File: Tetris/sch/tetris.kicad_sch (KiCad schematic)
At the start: 36 parts, among them J1 SWD, SW1 Boot, SW4 Reset, U1 CH32V203C8T6, U4 TLV70433DBVR

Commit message: PCB routing in progress
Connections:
- net LED/S1: now also U1.19 (PB1/ADC9); no longer U1.18 (PB0/ADC8)
- net LED/S2: now also U1.18 (PB0/ADC8); no longer U1.19 (PB1/ADC9)
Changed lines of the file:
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@@
 	(wire
 		(pts
-			(xy 236.22 110.49) (xy 232.41 110.49)
-		)
-		(stroke
-			(width 0)
-			(type default)
-		)
-	)
-	(wire
-		(pts
 			(xy 254 58.42) (xy 257.81 58.42)
 		)
@@
 	(wire
 		(pts
-			(xy 238.76 107.95) (xy 232.41 107.95)
+			(xy 200.66 77.47) (xy 214.63 77.47)
 		)
 		(stroke
@@
 	(wire
 		(pts
-			(xy 200.66 77.47) (xy 214.63 77.47)
+			(xy 147.32 102.87) (xy 149.86 102.87)
 		)
 		(stroke
@@
 	(wire
 		(pts
-			(xy 147.32 102.87) (xy 149.86 102.87)
+			(xy 224.79 58.42) (xy 224.79 45.72)
 		)
 		(stroke
@@
 	(wire
 		(pts
-			(xy 224.79 58.42) (xy 224.79 45.72)
+			(xy 269.24 58.42) (xy 269.24 62.23)
 		)
 		(stroke
@@
 	(wire
 		(pts
-			(xy 269.24 58.42) (xy 269.24 62.23)
+			(xy 232.41 110.49) (xy 236.22 110.49)
 		)
 		(stroke
@@
 	(wire
 		(pts
+			(xy 232.41 107.95) (xy 238.76 107.95)
+		)
+		(stroke
+			(width 0)
+			(type default)
+		)
+	)
+	(wire
+		(pts
 			(xy 163.83 87.63) (xy 163.83 77.47)
 		)
@@
 		)
 		(pin "S1" output
-			(at 232.41 107.95 0)
+			(at 232.41 110.49 0)
 			(effects
 				(font
@@
 		)
 		(pin "S2" output
-			(at 232.41 110.49 0)
+			(at 232.41 107.95 0)
 			(effects
 				(font

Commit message: Tetris PCB route in progress
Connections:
- net at U1.34 (PA13/SWDIO): now also J1.3 (Pin_3); no longer J1.4 (Pin_4)
- net at U1.37 (PA14/SWCLK): now also J1.4 (Pin_4); no longer J1.3 (Pin_3)
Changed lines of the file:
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@@
+	(wire
+		(pts
+			(xy 163.83 60.96) (xy 177.8 60.96)
+		)
+		(stroke
+			(width 0)
+			(type default)
+		)
+	)
 	(wire
 		(pts
@@
 	(wire
 		(pts
-			(xy 161.29 49.53) (xy 161.29 58.42)
-		)
-		(stroke
-			(width 0)
-			(type default)
-		)
-	)
-	(wire
-		(pts
 			(xy 147.32 80.01) (xy 151.13 80.01)
 		)
@@
 	(wire
 		(pts
+			(xy 50.8 185.42) (xy 50.8 186.69)
+		)
+		(stroke
+			(width 0)
+			(type default)
+		)
+	)
+	(wire
+		(pts
+			(xy 96.52 50.8) (xy 96.52 54.61)
+		)
+		(stroke
+			(width 0)
+			(type default)
+		)
+	)
+	(wire
+		(pts
+			(xy 163.83 92.71) (xy 167.64 92.71)
+		)
+		(stroke
+			(width 0)
+			(type default)
+		)
+	)
+	(wire
+		(pts
+			(xy 254 53.34) (xy 260.35 53.34)
+		)
+		(stroke
+			(width 0)
+			(type default)
+		)
+	)
+	(wire
+		(pts
+			(xy 66.04 186.69) (xy 50.8 186.69)
+		)
+		(stroke
+			(width 0)
+			(type default)
+		)
+	)
+	(wire
+		(pts
+			(xy 243.84 73.66) (xy 243.84 76.2)
+		)
+		(stroke
+			(width 0)
+			(type default)
+		)
+	)
+	(wire
+		(pts
+			(xy 121.92 54.61) (xy 121.92 49.53)
+		)
+		(stroke
+			(width 0)
+			(type default)
+		)
+	)
+	(wire
+		(pts
+			(xy 152.4 114.3) (xy 212.09 114.3)
+		)
+		(stroke
+			(width 0)
+			(type default)
+		)
+	)
+	(wire
+		(pts
+			(xy 66.04 90.17) (xy 68.58 90.17)
+		)
+		(stroke
+			(width 0)
+			(type default)
+		)
+	)
+	(wire
+		(pts
+			(xy 104.14 39.37) (xy 104.14 54.61)
+		)
+		(stroke
+			(width 0)
+			(type default)
+		)
+	)
+	(wire
+		(pts
+			(xy 238.76 30.48) (xy 238.76 26.67)
+		)
+		(stroke
+			(width 0)
+			(type default)
+		)
+	)
+	(wire
+		(pts
+			(xy 212.09 50.8) (xy 228.6 50.8)
+		)
+		(stroke
+			(width 0)
+			(type default)
+		)
+	)
+	(wire
+		(pts
+			(xy 66.04 92.71) (xy 68.58 92.71)
+		)
+		(stroke
+			(width 0)
+			(type default)
+		)
+	)
+	(wire
+		(pts
+			(xy 163.83 49.53) (xy 163.83 60.96)
+		)
+		(stroke
+			(width 0)
+			(type default)
+		)
+	)
+	(wire
+		(pts
+			(xy 36.83 161.29) (xy 63.5 161.29)
+		)
+		(stroke
+			(width 0)
+			(type default)
+		)
+	)
+	(wire
+		(pts
+			(xy 214.63 87.63) (xy 214.63 77.47)
+		)
+		(stroke
+			(width 0)
+			(type default)
+		)
+	)
+	(wire
+		(pts
+			(xy 111.76 133.35) (xy 111.76 154.94)
+		)
+		(stroke
+			(width 0)
+			(type default)
+		)
+	)
+	(wire
+		(pts
+			(xy 260.35 90.17) (xy 212.09 90.17)
+		)
+		(stroke
+			(width 0)
+			(type default)
+		)
+	)
+	(wire
+		(pts
+			(xy 222.25 17.78) (xy 222.25 45.72)
+		)
+		(stroke
+			(width 0)
+			(type default)
+		)
+	)
+	(wire
+		(pts
+			(xy 66.04 22.86) (xy 66.04 26.67)
+		)
+		(stroke
+			(width 0)
+			(type default)
+		)
+	)
+	(wire
+		(pts
 			(xy 161.29 58.42) (xy 177.8 58.42)
 		)
@@
 	(wire
 		(pts
-			(xy 50.8 185.42) (xy 50.8 186.69)
-		)
-		(stroke
-			(width 0)
-			(type default)
-		)
-	)
-	(wire
-		(pts
-			(xy 96.52 50.8) (xy 96.52 54.61)
-		)
-		(stroke
-			(width 0)
-			(type default)
-		)
-	)
-	(wire
-		(pts
-			(xy 163.83 92.71) (xy 167.64 92.71)
-		)
-		(stroke
-			(width 0)
-			(type default)
-		)
-	)
-	(wire
-		(pts
-			(xy 254 53.34) (xy 260.35 53.34)
-		)
-		(stroke
-			(width 0)
-			(type default)
-		)
-	)
-	(wire
-		(pts
-			(xy 66.04 186.69) (xy 50.8 186.69)
-		)
-		(stroke
-			(width 0)
-			(type default)
-		)
-	)
-	(wire
-		(pts
-			(xy 243.84 73.66) (xy 243.84 76.2)
-		)
-		(stroke
-			(width 0)
-			(type default)
-		)
-	)
-	(wire
-		(pts
-			(xy 121.92 54.61) (xy 121.92 49.53)
-		)
-		(stroke
-			(width 0)
-			(type default)
-		)
-	)
-	(wire
-		(pts
-			(xy 152.4 114.3) (xy 212.09 114.3)
-		)
-		(stroke
-			(width 0)
-			(type default)
-		)
-	)
-	(wire
-		(pts
-			(xy 66.04 90.17) (xy 68.58 90.17)
-		)
-		(stroke
-			(width 0)
-			(type default)
-		)
-	)
-	(wire
-		(pts
-			(xy 104.14 39.37) (xy 104.14 54.61)
-		)
-		(stroke
-			(width 0)
-			(type default)
-		)
-	)
-	(wire
-		(pts
-			(xy 238.76 30.48) (xy 238.76 26.67)
-		)
-		(stroke
-			(width 0)
-			(type default)
-		)
-	)
-	(wire
-		(pts
-			(xy 212.09 50.8) (xy 228.6 50.8)
-		)
-		(stroke
-			(width 0)
-			(type default)
-		)
-	)
-	(wire
-		(pts
-			(xy 66.04 92.71) (xy 68.58 92.71)
-		)
-		(stroke
-			(width 0)
-			(type default)
-		)
-	)
-	(wire
-		(pts
-			(xy 36.83 161.29) (xy 63.5 161.29)
-		)
-		(stroke
-			(width 0)
-			(type default)
-		)
-	)
-	(wire
-		(pts
-			(xy 214.63 87.63) (xy 214.63 77.47)
-		)
-		(stroke
-			(width 0)
-			(type default)
-		)
-	)
-	(wire
-		(pts
-			(xy 111.76 133.35) (xy 111.76 154.94)
-		)
-		(stroke
-			(width 0)
-			(type default)
-		)
-	)
-	(wire
-		(pts
-			(xy 260.35 90.17) (xy 212.09 90.17)
-		)
-		(stroke
-			(width 0)
-			(type default)
-		)
-	)
-	(wire
-		(pts
-			(xy 222.25 17.78) (xy 222.25 45.72)
-		)
-		(stroke
-			(width 0)
-			(type default)
-		)
-	)
-	(wire
-		(pts
-			(xy 66.04 22.86) (xy 66.04 26.67)
-		)
-		(stroke
-			(width 0)
-			(type default)
-		)
-	)
-	(wire
-		(pts
 			(xy 66.04 184.15) (xy 66.04 186.69)
 		)
@@
 	(wire
 		(pts
-			(xy 161.29 85.09) (xy 161.29 60.96)
+			(xy 161.29 58.42) (xy 161.29 85.09)
 		)
 		(stroke
@@
 	(wire
 		(pts
-			(xy 121.92 49.53) (xy 161.29 49.53)
+			(xy 121.92 49.53) (xy 163.83 49.53)
 		)
 		(stroke
@@
 		)
 		(stroke
-			(width 0)
-			(type default)
-		)
-	)
-	(wire
-		(pts
-			(xy 161.29 60.96) (xy 177.8 60.96)
-		)
-		(stroke

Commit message: PCB is ready
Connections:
- net Btns/B2: now also U1.15 (PA5/ADC5); no longer U1.11 (PA1/ADC1)
- net Btns/B3: now also U1.13 (PA3/ADC3); no longer U1.12 (PA2/ADC2)
- net Btns/B4: now also U1.12 (PA2/ADC2); no longer U1.13 (PA3/ADC3)
- net Btns/B5: now also U1.11 (PA1/ADC1); no longer U1.14 (PA4/ADC4)
- net Btns/B6: now also U1.16 (PA6/ADC6); no longer U1.15 (PA5/ADC5)
- net Btns/B7: now also U1.14 (PA4/ADC4); no longer U1.16 (PA6/ADC6)
- no-connect marks 0 -> 2
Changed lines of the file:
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@@
 		(color 0 0 0 0)
 	)
+	(no_connect
+		(at 254 55.88)
+	)
+	(no_connect
+		(at 228.6 48.26)
+	)
 	(wire
 		(pts
@@
 		)
 		(pin "B2" output
-			(at 78.74 149.86 180)
+			(at 99.06 142.24 90)
 			(effects
 				(font
 					(size 1.27 1.27)
 				)
-				(justify left)
+				(justify right)
 			)
 		)
 		(pin "B3" output
-			(at 78.74 147.32 180)
+			(at 93.98 142.24 90)
 			(effects
 				(font
 					(size 1.27 1.27)
 				)
-				(justify left)
+				(justify right)
 			)
 		)
 		(pin "B4" output
-			(at 93.98 142.24 90)
+			(at 78.74 147.32 180)
 			(effects
 				(font
 					(size 1.27 1.27)
 				)
-				(justify right)
+				(justify left)
 			)
 		)
 		(pin "B5" output
-			(at 96.52 142.24 90)
+			(at 78.74 149.86 180)
 			(effects
 				(font
 					(size 1.27 1.27)
 				)
-				(justify right)
+				(justify left)
 			)
 		)
 		(pin "B6" output
-			(at 99.06 142.24 90)
+			(at 101.6 142.24 90)
 			(effects
 				(font
@@
 		)
 		(pin "B7" output
-			(at 101.6 142.24 90)
+			(at 96.52 142.24 90)
 			(effects
 				(font

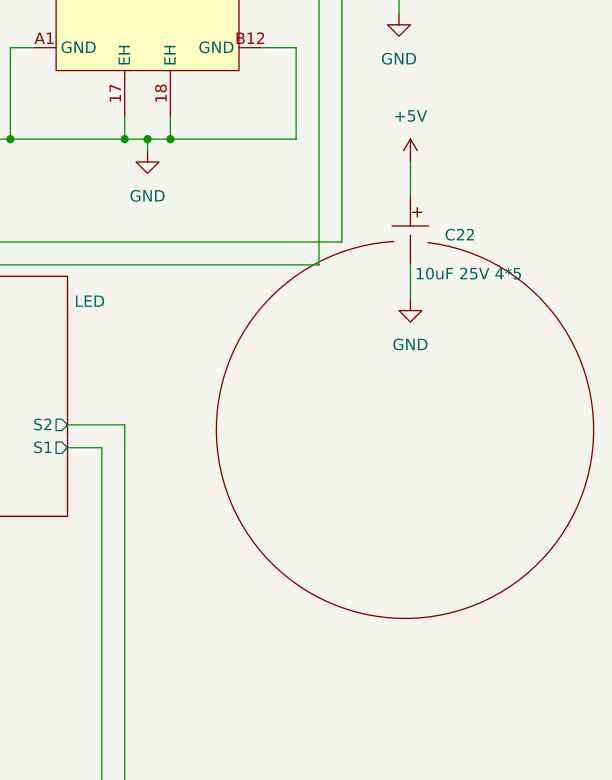
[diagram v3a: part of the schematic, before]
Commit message: Updated V ADJ resistor value. Fixed capacitor symbol in PDF
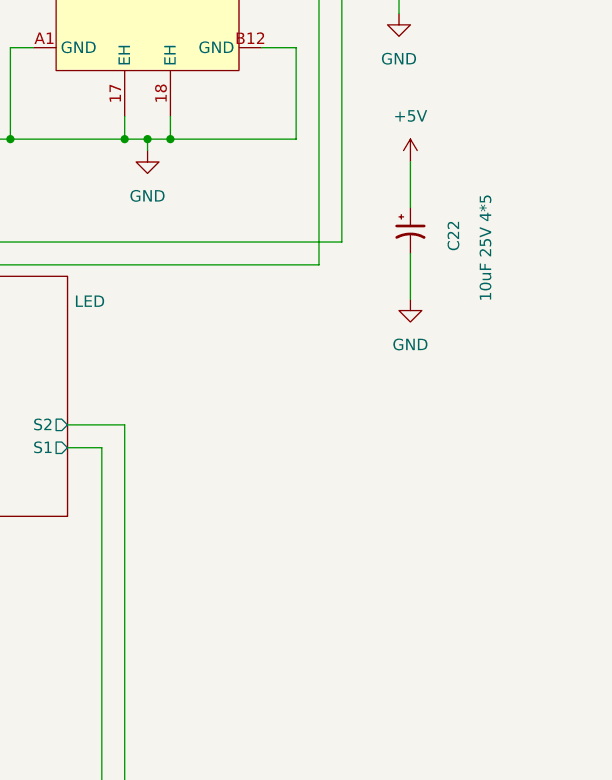
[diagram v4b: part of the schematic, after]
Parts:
- C22: symbol EasyEDA:10uF25V4*5 -> Device:C_Polarized_Small_US
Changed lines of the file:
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@@
 	(wire
 		(pts
-			(xy 270.51 78.74) (xy 270.51 82.55)
+			(xy 270.51 78.74) (xy 270.51 83.82)
 		)
 		(stroke
@@
 	(wire
 		(pts
-			(xy 270.51 90.17) (xy 270.51 93.98)
+			(xy 270.51 88.9) (xy 270.51 93.98)
 		)
 		(stroke
@@
 	)
 	(symbol
-		(lib_id "EasyEDA:10uF25V4*5")
-		(at 270.51 86.36 270)
+		(lib_id "Device:C_Polarized_Small_US")
+		(at 270.51 86.36 0)
 		(unit 1)
 		(exclude_from_sim no)
@@
 		(dnp no)
 		(property "Reference" "C22"
-			(at 274.32 86.868 90)
+			(at 275.336 88.646 90)
 			(effects
 				(font
@@
 		)
 		(property "Value" "10uF 25V 4*5"
-			(at 271.018 91.186 90)
+			(at 278.892 94.234 90)
 			(effects
 				(font
@@
 		)
 		(property "Footprint" "easyeda2kicad:CAP-TH_BD4.0-P1.50-D0.8-FD"
-			(at 262.89 86.36 0)
+			(at 270.51 93.98 0)
 			(effects
 				(font
@@
 		)
 		(property "Datasheet" "https://lcsc.com/product-detail/Aluminum-Electrolytic-Capacitors-Leaded_10uF-25V_C43846.html"
-			(at 260.35 86.36 0)
+			(at 270.51 96.52 0)
 			(effects
 				(font
@@
 		)
 		(property "LCSC Part" "C43846"
-			(at 257.81 86.36 0)
+			(at 270.51 99.06 0)
 			(effects
 				(font
